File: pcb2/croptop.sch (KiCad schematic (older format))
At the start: 0 parts

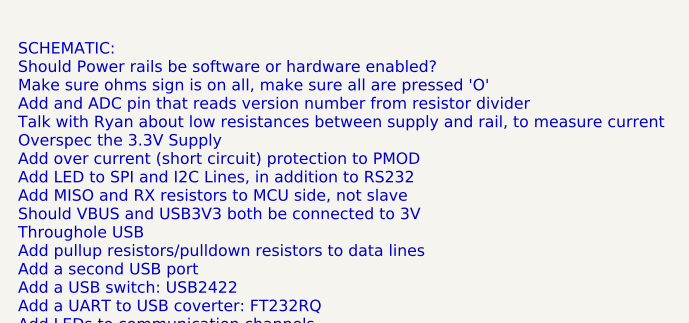
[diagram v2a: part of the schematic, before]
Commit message: Added pmod
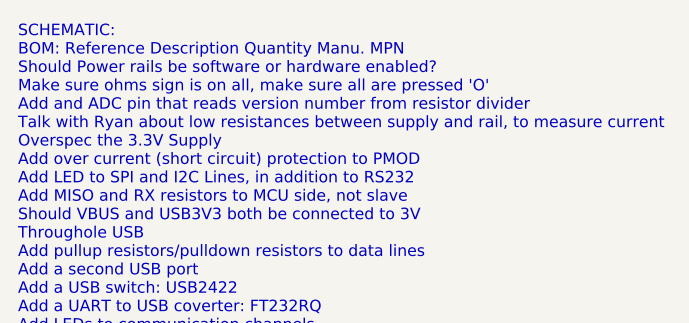
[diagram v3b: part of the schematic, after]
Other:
- note added: "SCHEMATIC:\nBOM: Reference Description Quantity Manu. MPN\nShould Power rails be software or hardware enabled?\nMake sure ohms sign is on all, make sure all are pressed 'O'\nAdd and ADC pin that reads version number from resistor divider\nTalk with Ryan about low resistances between supply and rail, to measure current\nOverspec the 3.3V Supply\nAdd over current (short circuit) protection to PMOD\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"
- note removed: "SCHEMATIC:\nShould Power rails be software or hardware enabled?\nMake sure ohms sign is on all, make sure all are pressed 'O'\nAdd and ADC pin that reads version number from resistor divider\nTalk with Ryan about low resistances between supply and rail, to measure current\nOverspec the 3.3V Supply\nAdd over current (short circuit) protection to PMOD\nAdd LED to SPI and I2C Lines, in addition to R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"
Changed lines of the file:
@@
 encoding utf-8
 Sheet 1 6
-Title "CropTop"
-Date "2018-11-20"
-Rev "Revision 8"
+Title "CropTop 2.0"
+Date "2019-03-18"
+Rev "Revision 12"
 Comp "University of Idaho"
 Comment1 "Kennedy Caisley, Ryan Donahue"
@@
 System Block Diagram
 Text Notes 1250 7850 0    50   ~ 0
-SCHEMATIC:\nShould Power rails be software or hardware enabled?\nMake sure ohms sign is on all, make sure all are pressed 'O'\nAdd and ADC pin that reads version number from resistor divider\nTalk with Ryan about low resistances between supply and rail, to measure current\nOverspec the 3.3V Supply\nAdd over current (short circuit) protection to PMOD\nAdd LED to SPI and I2C Lines, in addition to RS232\nAdd MISO and RX resistors to MCU side, not slave\nShould VBUS and USB3V3 both be connected to 3V\nThroughole USB\nAdd pullup resistors/pulldown resistors to data lines\nAdd a second USB port\nAdd a USB switch: USB2422\nAdd a UART to USB coverter: FT232RQ\nAdd LEDs to communication channels\nAdd Series resistors to comm lines, allowing the resistor to be changed\nAdd A4988 stepper motor driver\nAdd GPIO Block with ESD protection\nAdd SPI/UART/I2C with ESD potection on terminal blocks\nAdd a stepper motor driver\nAdd an audio circuit to the FTDI chip (recommends TPA6205A1)\nAdd enough notes that even an ME can understand the circuit\nAdd missing pullups and pulldowns on temp/memory\nAdd MISO to SPI bus\nAdd resistor to Load bank for current limit\nSeries resistors: (220=20ns delay, 22=5ns delay) (or 10Mhz vs 100Mhz)\nAdd address of components to sheet\nMore protection on motor and stepper? (Stepper pg. 15)\nMake location of resistor value consistent (inside vs. outside)\nMake sure all devices have testpoint in any useful places\nChange AVDD to 5V0_REG, DVDD to 3V3\nAdd inductor to ADC\nChange nets to have directions\nRemove global nets on power\nSplit memory and adc spi bus\nAdd datasheets for components into schematic\nAdd configurable voltage to IO ports\nMove testpoints onto schematic\nMake sure all global nets are facing right direciton\nMake sure all LED resistors are selected\nDoes DRV_FLT need a pull up?\nCheck if DC and Stepper motor needs external flyback diodes\nChange accellerometer to gyro L3GD20H\nRemove buffer from ADC\nFigure out whether off board peripherals need buffer\nMake sure all CAP on motor drivers are at least 50V Rated\nCan Stepper motor driver use 3.3V for REF?\nChange name of I2C and SPI and RS232 to add numbers and what bus? (tx -> I2C_TX_1)\nMove ADC and NAND to different SPI Buses\nMake NAND 1GB instead of 1Gb\nFillout partnumber and datasheet for all components\nGive all devices a 10uF and 0.1uF (100nF) capacitor, at the very least\n\nPCB:\nAll elements that have a pad, make sure that there is a pad pin and it's footprint is has the pad assigned to it\nCheck that all components with a pad are connected with solder paste in footprint\nAdd a cut out around temperature sensor\nAdd vias to mounting holes for style\nMake logo in copper layer, not silkscreen\nHow do I route a 90 ohm USB trace\nPut croptop sign in copper layer\nMove ADC over star ground\nMove memory and ADC to different busses\nAdd heat sinks to motor drivers\nGround plane on top and bottom layer\nLook into thermal vias for motor drivers\nAdd silkscreen labels to configuration resistors\nWhen laying out the footprint for the motor drivers, follow datasheet\nMove micro usb and lcd connector further forward\nAdd ground plane to top and bottom layers\nStitch top and bottom layers together with vias\nSPI I2C and RS232 testpoints should be closer to pic, or at fork point\nLabel Terminal blocks on top side\n\nCOMPLETION STEPS:\nManually check entire board with Ryan, with each datasheet\nCalculate power rail burdens\nFigure out if ESD diodes will mess up ADC measurements\nCome up with different devices configurations (using DNP for components)\nRun through pin out of every chip and verify it's connection\nVerify the package footprint of every chip\nMake sure that 3V3 rotary encoder buffer resistor is DNP\n
+SCHEMATIC:\nBOM: Reference Description Quantity Manu. MPN\nShould Power rails be software or hardware enabled?\nMake sure ohms sign is on all, make sure all are pressed 'O'\nAdd and ADC pin that reads version number from resistor divider\nTalk with Ryan about low resistances between supply and rail, to measure current\nOverspec the 3.3V Supply\nAdd over current (short circuit) protection to PMOD\nAdd LED to SPI and I2C Lines, in addition to RS232\nAdd MISO and RX resistors to MCU side, not slave\nShould VBUS and USB3V3 both be connected to 3V\nThroughole USB\nAdd pullup resistors/pulldown resistors to data lines\nAdd a second USB port\nAdd a USB switch: USB2422\nAdd a UART to USB coverter: FT232RQ\nAdd LEDs to communication channels\nAdd Series resistors to comm lines, allowing the resistor to be changed\nAdd A4988 stepper motor driver\nAdd GPIO Block with ESD protection\nAdd SPI/UART/I2C with ESD potection on terminal blocks\nAdd a stepper motor driver\nAdd an audio circuit to the FTDI chip (recommends TPA6205A1)\nAdd enough notes that even an ME can understand the circuit\nAdd missing pullups and pulldowns on temp/memory\nAdd MISO to SPI bus\nAdd resistor to Load bank for current limit\nSeries resistors: (220=20ns delay, 22=5ns delay) (or 10Mhz vs 100Mhz)\nAdd address of components to sheet\nMore protection on motor and stepper? (Stepper pg. 15)\nMake location of resistor value consistent (inside vs. outside)\nMake sure all devices have testpoint in any useful places\nChange AVDD to 5V0_REG, DVDD to 3V3\nAdd inductor to ADC\nChange nets to have directions\nRemove global nets on power\nSplit memory and adc spi bus\nAdd datasheets for components into schematic\nAdd configurable voltage to IO ports\nMove testpoints onto schematic\nMake sure all global nets are facing right direciton\nMake sure all LED resistors are selected\nDoes DRV_FLT need a pull up?\nCheck if DC and Stepper motor needs external flyback diodes\nChange accellerometer to gyro L3GD20H\nRemove buffer from ADC\nFigure out whether off board peripherals need buffer\nMake sure all CAP on motor drivers are at least 50V Rated\nCan Stepper motor driver use 3.3V for REF?\nChange name of I2C and SPI and RS232 to add numbers and what bus? (tx -> I2C_TX_1)\nMove ADC and NAND to different SPI Buses\nMake NAND 1GB instead of 1Gb\nFillout partnumber and datasheet for all components\nGive all devices a 10uF and 0.1uF (100nF) capacitor, at the very least\n\nPCB:\nAll elements that have a pad, make sure that there is a pad pin and it's footprint is has the pad assigned to it\nCheck that all components with a pad are connected with solder paste in footprint\nAdd a cut out around temperature sensor\nAdd vias to mounting holes for style\nMake logo in copper layer, not silkscreen\nHow do I route a 90 ohm USB trace\nPut croptop sign in copper layer\nMove ADC over star ground\nMove memory and ADC to different busses\nAdd heat sinks to motor drivers\nGround plane on top and bottom layer\nLook into thermal vias for motor drivers\nAdd silkscreen labels to configuration resistors\nWhen laying out the footprint for the motor drivers, follow datasheet\nMove micro usb and lcd connector further forward\nAdd ground plane to top and bottom layers\nStitch top and bottom layers together with vias\nSPI I2C and RS232 testpoints should be closer to pic, or at fork point\nLabel Terminal blocks on top side\n\nCOMPLETION STEPS:\nManually check entire board with Ryan, with each datasheet\nCalculate power rail burdens\nFigure out if ESD diodes will mess up ADC measurements\nCome up with different devices configurations (using DNP for components)\nRun through pin out of every chip and verify it's connection\nVerify the package footprint of every chip\nMake sure that 3V3 rotary encoder buffer resistor is DNP\n
 $EndSCHEMATC
